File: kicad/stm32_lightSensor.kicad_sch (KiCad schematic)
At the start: 4 parts, among them J1 Conn_02x19_Odd_Even, J2 Conn_02x19_Odd_Even, U1 NUCLEO-F446RE

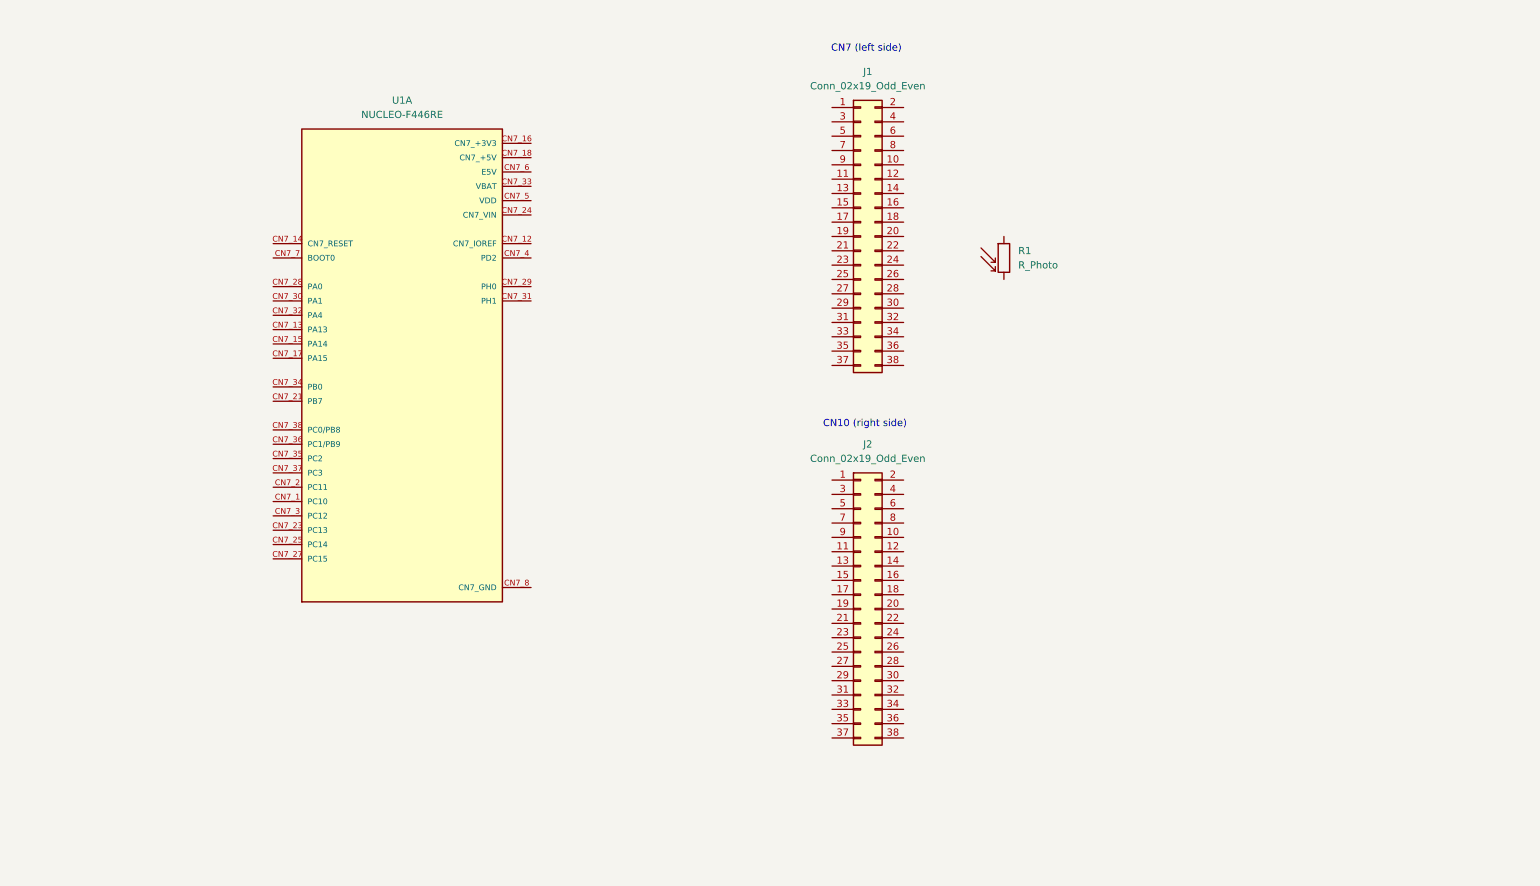
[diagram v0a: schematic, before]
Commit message: started working on voltage divider for LDR
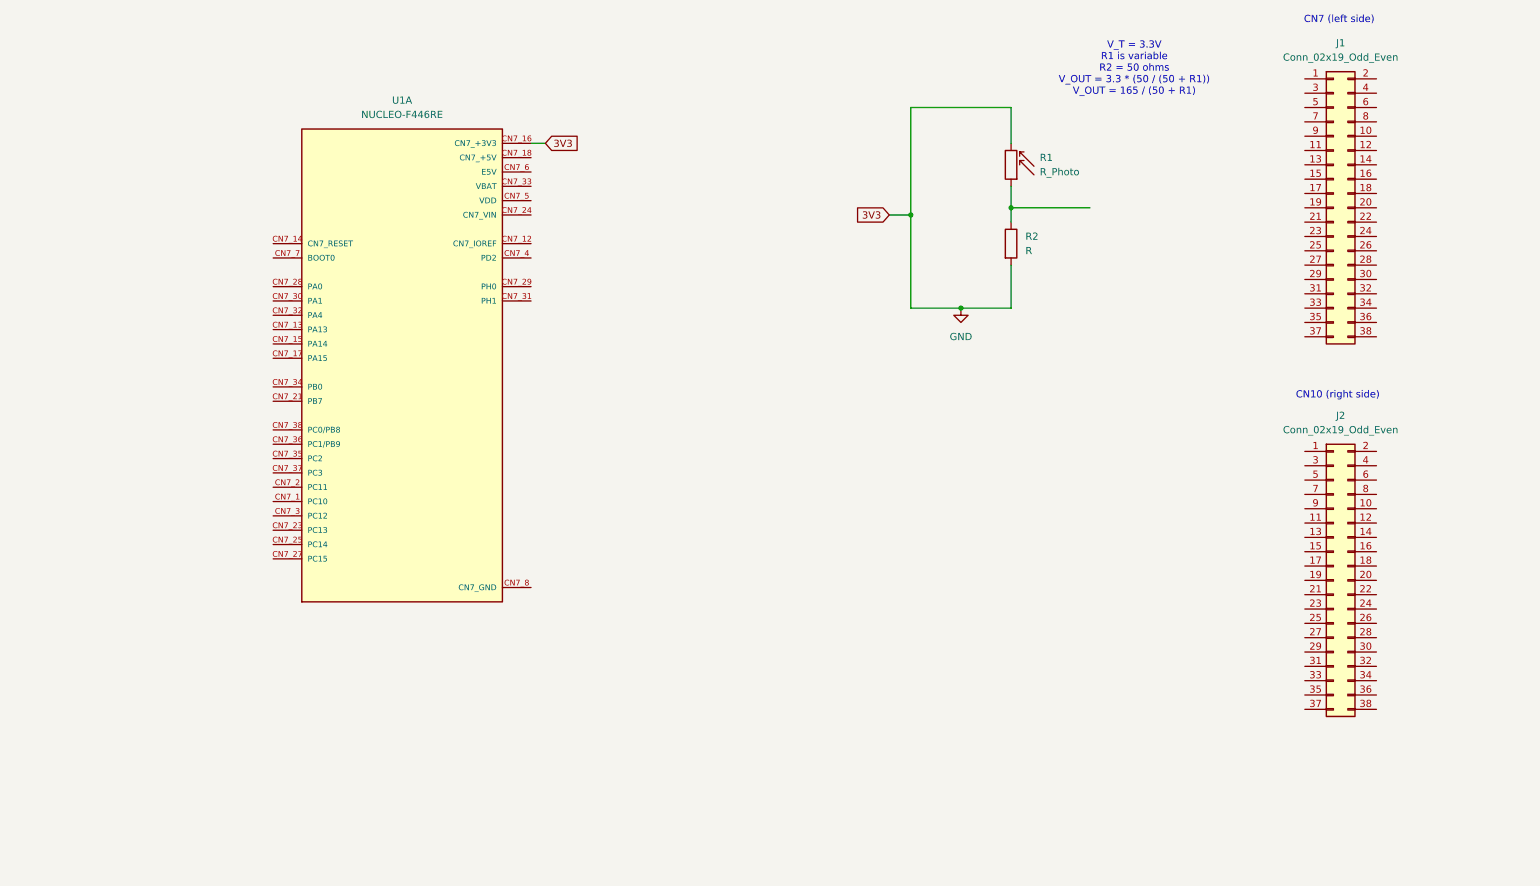
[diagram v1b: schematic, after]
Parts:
- added R2: R, symbol Device:R
- U1: datasheet_chip (none) -> https://www.st.com/resource/en/datasheet/stm32f446mc.pdf
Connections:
- net GND: now reaches U1.CN7_16 (CN7_+3V3)
- net GND: now also R1.2, R2.2
- net at R1.1: now also R2.1
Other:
- note added: "V_T = 3.3V R1 is variable R2 = 50 ohms V_OUT = 3.3 * (50 / (50 + R1)) V_OUT = 165 / (50 + R1)"
- moved on the sheet: J1, J2, R1

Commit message: finishing project at decent stopping point
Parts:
- added C1: 1 uF, symbol Device:C
- added R3: 10k ohms, symbol Device:R
- added U2: TLV9062xD, Package_SO:SOIC-8_3.9x4.9mm_P1.27mm, symbol Amplifier_Operational:TLV9062xD
- R2: value R -> 50 ohms
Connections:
- net GND: now also C1.1
- net at R1.1, R2.1: now also U2.3 (+)
- new net: R3.1, U2.1, U2.2 (-)
- new net PA0: C1.2, R3.2
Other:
- note added: "50 ohm resistor in divider wastes current -> should be replaced, but I have decided this schematic is not going to fabrication, so leaving it as is"
- note added: "RC Filter (low pass): Cut-off frequency: 20 hz 20 = R*C = 1 / (2 pi * 20) R = 10k ohms C = 0.8 microfarads ~= 1 microfarad"
- note added: "Voltage follower decouples divider and RC + ADC circuits Prevents divider's series resistance from coupling w/ RC low-pass filter"
- moved on the sheet: J1, J2
